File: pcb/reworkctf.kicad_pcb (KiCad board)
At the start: 4 copper layers, 45 x 60 mm, 135 parts, among them J1 XILINX_JTAG, J2 UX60SX-MB-5ST, U1 XC3S50A-4FTG256C, U2 W25Q80BV, U3 74HC04, U4 1 MHz, U5 ADP322ACPZ-145-R7, U6 74HC04

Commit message: Continued initial layout
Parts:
- added G***: LOGO, w_logo:Logo_silk_WEEE_3.4x5mm, F.Cu at (43.0, 21.0)
- added G***: LOGO, w_logo:Logo_silk_ROHS_5x2.8mm, F.Cu at (38.0, 22.0)
- added G***: LOGO, w_logo:Logo_silk_OSHW_6x6mm, F.Cu at (49.0, 20.0)
- added G***: LOGO, azonenberg_pcb:LONGTHING-1200DPI, F.Cu at (33.0, 62.0)
- added R52: 1K, azonenberg_pcb:EIA_0402_RES_NOSILK, F.Cu at (85.6, 52.0)
- added REF**: MECHANICAL_CLEARANCEHOLE_4_40, azonenberg_pcb:MECHANICAL_CLEARANCEHOLE_4_40, F.Cu at (95.0, 71.0)
- added REF**: MECHANICAL_CLEARANCEHOLE_4_40, azonenberg_pcb:MECHANICAL_CLEARANCEHOLE_4_40, F.Cu at (95.0, 21.0)
- C13, C14, C15, C16, C28, C45, R1, R10, R2, R3, R4, R5, R6, R7, R8, R9: moved to B.Cu
- moved R6 88.5 mm to (61.5, 56.5)
- moved R9 78.5 mm to (64.0, 59.0)
- moved R3 73.8 mm to (71.5, 59.5)
- moved R1 71.2 mm to (55.0, 56.0)
- moved R7 68.9 mm to (63.9, 56.5)
- moved R8 68.8 mm to (66.5, 56.5)
- moved R2 68.3 mm to (60.5, 58.0)
- moved R5 64.7 mm to (59.0, 56.0)
- moved R10 62.1 mm to (67.0, 59.5)
- moved R29 59.1 mm to (90.5, 46.5)
- moved R4 59.1 mm to (71.0, 58.0)
- moved C16 52.3 mm to (57.0, 46.0), turned to 180 degrees
- moved C18 52.1 mm to (43.5, 45.5)
- moved C26 47.6 mm to (105.5, 19.5)
- moved C15 46.4 mm to (59.5, 51.5), turned to 180 degrees
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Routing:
- net /GND: track 313.6 -> 317.8 mm, vias 60 -> 62
- net /3V3: track 83.3 -> 85.5 mm
- net /2V5: track 87.2 -> 87.7 mm
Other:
- board size 45 x 60 mm -> 75 x 60 mm
- board text added: "Rework Challenge v0.1 A. Zonenberg / 2017-05-23"

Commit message: Continued work on initial layout
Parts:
- R3, R4, R7, R8: moved to F.Cu
- moved U3 42.0 mm to (83.0, 36.5)
- moved C18 42.0 mm to (83.0, 31.2)
- moved R1 20.0 mm to (55.0, 36.0), turned to 270 degrees
- moved R2 19.8 mm to (57.0, 38.5), turned to 90 degrees
- moved R9 12.9 mm to (55.2, 49.5)
- moved R8 12.1 mm to (54.5, 55.2), turned to 90 degrees
- moved R10 11.7 mm to (56.5, 54.2), turned to 90 degrees
- moved R3 8.56 mm to (72.5, 51.0)
- moved R7 8.00 mm to (56.0, 55.2), turned to 90 degrees
- moved R4 6.60 mm to (65.0, 55.2), turned to 90 degrees
- moved R6 4.07 mm to (57.5, 55.8), turned to 90 degrees
- moved R5 3.16 mm to (58.0, 53.0), turned to 90 degrees
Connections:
- U1 pad C1: /LEVEL22_OK -> /LEVEL1_OK
- U1 pad D1: /LEVEL17_OK -> /LEVEL2_OK
- U1 pad D3: /LEVEL20_OK -> /LEVEL3_OK
- U1 pad D4: /LEVEL19_OK -> /LEVEL9_TEST
- U1 pad E1: /LEVEL18_OK -> /LEVEL4_OK
- U1 pad F1: Net-(R39-Pad2) -> /LEVEL5_OK
- U1 pad F3: /LEVEL9_TEST -> /LEVEL6_OK
- U1 pad G1: /LEVEL8_TEST -> /LEVEL7_OK
- U1 pad G2: /LEVEL15_OK -> /LEVEL8_TEST
- U1 pad G3: Net-(R30-Pad2) -> Net-(U1-PadG3)
- U1 pad H1: /LEVEL16_OK -> /LEVEL8_OK
- U1 pad H3: /LEVEL13_OK -> /LEVEL9_OK
- U1 pad H4: Net-(R38-Pad2) -> Net-(U1-PadH4)
- U1 pad H5: /LEVEL3_TEST -> Net-(U1-PadH5)
- U1 pad H6: Net-(R31-Pad2) -> Net-(U1-PadH6)
- U1 pad J1: /LEVEL12_OK -> /LEVEL10_OK
- U1 pad J3: /LEVEL14_OK -> Net-(U1-PadJ3)
- U1 pad K1: /LEVEL10_OK -> /LEVEL12_OK
- U1 pad K3: /LEVEL9_OK -> /LEVEL13_OK
- U1 pad M1: /LEVEL7_OK -> /LEVEL14_OK
- U1 pad M4: /LEVEL2_OK -> /LEVEL20_OK
- U1 pad N1: /LEVEL8_OK -> /LEVEL15_OK
- U1 pad N2: /LEVEL5_OK -> /LEVEL16_OK
- U1 pad N3: /LEVEL1_OK -> /LEVEL22_OK
- U1 pad P1: /LEVEL6_OK -> /LEVEL17_OK
- U1 pad P2: /LEVEL4_OK -> /LEVEL18_OK
- U1 pad R1: /LEVEL3_OK -> /LEVEL19_OK
- U1 pad R5: Net-(U1-PadR5) -> Net-(R38-Pad2)
- U1 pad R9: Net-(U1-PadR9) -> Net-(R31-Pad2)
- U1 pad T10: Net-(U1-PadT10) -> Net-(R39-Pad2)
- U1 pad T4: Net-(U1-PadT4) -> Net-(R30-Pad2)
- U1 pad T9: Net-(U1-PadT9) -> /LEVEL3_TEST
- U3 pad 8: /LEVEL4_TEST -> /LEVEL4_SENSE
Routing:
- net /JTAG_TDO: track 0.00 -> 46.1 mm, vias 0 -> 3
- net /JTAG_TCK: track 0.00 -> 44.4 mm, vias 0 -> 3
- net /FPGA_DONE: track 0.00 -> 38.4 mm, vias 0 -> 4
- net /LEVEL18_OK: track 0.00 -> 38.2 mm
- net /LEVEL13_OK: track 0.00 -> 37.9 mm
- net /LEVEL19_OK: track 0.00 -> 37.5 mm
- net /LEVEL16_OK: track 0.00 -> 37.2 mm
- net /LEVEL11_OK: track 0.00 -> 36.2 mm
- net /LEVEL17_OK: track 0.00 -> 36.0 mm
- net /LEVEL9_OK: track 0.00 -> 35.9 mm
- net /LEVEL14_OK: track 0.00 -> 35.5 mm
- net /LEVEL12_OK: track 0.00 -> 35.5 mm
- net /LEVEL15_OK: track 0.00 -> 35.2 mm
- net /LEVEL6_OK: track 0.00 -> 34.9 mm
- net /LEVEL10_OK: track 0.00 -> 34.3 mm
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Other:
- board text added: "PCB Rework Challenge v0.1 A. Zonenberg / 2017-05-23"
- board text removed: "Rework Challenge v0.1 A. Zonenberg / 2017-05-23"

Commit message: Began work on active mesh
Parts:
- moved U2 9.33 mm to (82.2, 58.8)
- moved C17 7.52 mm to (87.5, 55.8)
- moved R28 7.52 mm to (86.9, 52.2)
- moved R29 7.52 mm to (92.5, 53.8)
- moved R52 7.52 mm to (87.6, 59.2)
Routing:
- net /GND: track 330.9 -> 540.0 mm, vias 65 -> 163
- net /LEVEL22_OK: track 0.00 -> 27.4 mm, vias 0 -> 1
- net /LEVEL21_OK: track 0.00 -> 26.2 mm, vias 0 -> 1
- net /LEVEL20_OK: track 0.00 -> 24.4 mm, vias 0 -> 1
- net /LEVEL5_OK: track 32.2 -> 50.1 mm
- net /LEVEL2_OK: track 31.0 -> 48.8 mm
- net /LEVEL4_OK: track 32.0 -> 49.6 mm
- net /LEVEL3_OK: track 33.9 -> 51.4 mm
- net /LEVEL1_OK: track 31.2 -> 48.3 mm
- net /SPI_MISO: track 7.75 -> 23.7 mm
- net /SPI_MOSI: track 16.5 -> 31.1 mm
- net /LEVEL6_OK: track 34.9 -> 49.2 mm
- net /LEVEL7_OK: track 33.2 -> 46.7 mm
- net /LEVEL8_OK: track 33.5 -> 46.0 mm
- net /SPI_SCK: track 9.46 -> 21.9 mm
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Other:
- rule via_min_size: 0.55 -> 0.475
- board text added: "PCB Rework Challenge v0.1 A. Zonenberg / 2017-05-24"
- board text removed: "PCB Rework Challenge v0.1 A. Zonenberg / 2017-05-23"

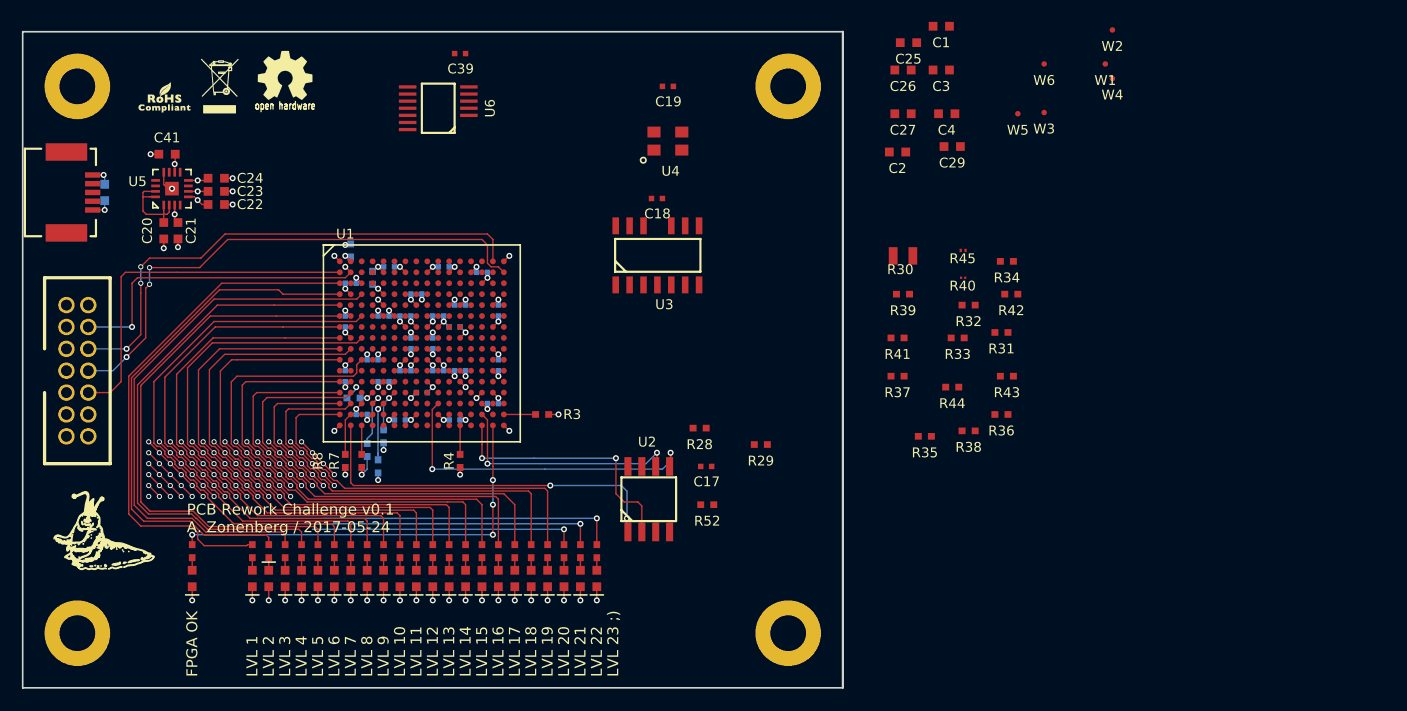
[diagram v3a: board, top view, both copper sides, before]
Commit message: Finished initial work on rework challenge board
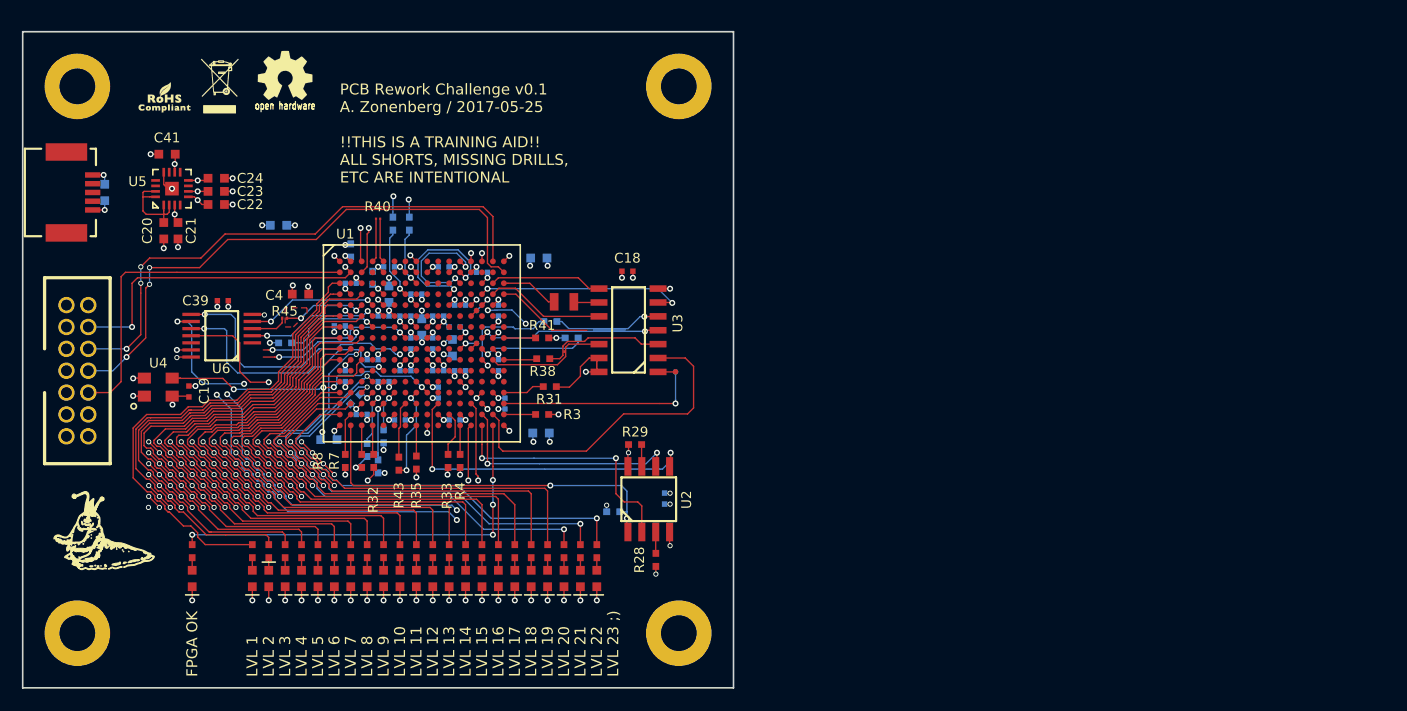
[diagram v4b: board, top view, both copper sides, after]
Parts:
- removed R34: 270, azonenberg_pcb:EIA_0402_RES_NOSILK
- added LEVEL2_SHORT: TESTPOINT_BARETRACE_150UM, azonenberg_pcb:TESTPOINT_BARETRACE_150UM, F.Cu at (77.5, 46.5)
- added LEVEL5_SHORT: TESTPOINT_BARETRACE_150UM, azonenberg_pcb:TESTPOINT_BARETRACE_150UM, F.Cu at (74.5, 45.2)
- added LEVEL6_SHORT: TESTPOINT_BARETRACE_150UM, azonenberg_pcb:TESTPOINT_BARETRACE_150UM, B.Cu at (78.7, 43.3)
- C1, C17, C2, C25, C26, C27, C29, C3, R36, R37, R39, R44, R52, W1, W2, W5: moved to B.Cu
- R41: value 0 -> 270
- R42: value 0 -> 270; moved to B.Cu
- moved C3 65.4 mm to (53.0, 53.3)
- moved W2 63.6 mm to (66.5, 41.5)
- moved W1 62.9 mm to (66.5, 44.5)
- moved R45 62.4 mm to (49.0, 42.2)
- moved W4 61.9 mm to (66.5, 41.5)
- moved C4 61.4 mm to (50.4, 40.0)
- moved R44 61.1 mm to (49.0, 44.5)
- moved C27 58.0 mm to (48.4, 33.7)
- moved R36 56.9 mm to (60.4, 33.5), turned to 270 degrees
- moved R32 56.2 mm to (57.1, 55.2), turned to 90 degrees
- moved R43 56.2 mm to (59.4, 55.5), turned to 90 degrees
- moved W3 56.0 mm to (66.5, 44.5)
- moved R40 53.8 mm to (57.5, 33.1)
- moved C19 51.9 mm to (40.2, 48.9), turned to 90 degrees
- moved U4 51.7 mm to (37.4, 48.5)
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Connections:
- R30 pad 1: /LEVEL4_TEST -> Net-(R30-Pad1)
- R30 pad 2: Net-(R30-Pad2) -> /LEVEL4_TEST
- R32 pad 1: Net-(R32-Pad1) -> /LEVEL16_TEST_A
- R32 pad 2: /LEVEL16_TEST_A -> Net-(R32-Pad2)
- R33 pad 1: Net-(R33-Pad1) -> /LEVEL16_TEST_B
- R33 pad 2: /LEVEL16_TEST_B -> Net-(R33-Pad2)
- R35 pad 1: Net-(R35-Pad1) -> /LEVEL21_TEST
- R35 pad 2: /LEVEL21_TEST -> Net-(R35-Pad2)
- R40 pad 1: /LEVEL9_SENSE -> /LEVEL9_TEST
- R40 pad 2: /LEVEL9_TEST -> /LEVEL9_SENSE
- R41 pad 1: /LEVEL19_SENSE -> Net-(R41-Pad1)
- U1 pad A11: /LEVEL15_TEST_N -> Net-(U1-PadA11)
- U1 pad A12: Net-(U1-PadA12) -> /LEVEL7_TEST_N
- U1 pad A13: Net-(U1-PadA13) -> /LEVEL15_TEST_N
- U1 pad A14: Net-(U1-PadA14) -> /LEVEL15_TEST_P
- U1 pad A3: Net-(U1-PadA3) -> /LEVEL13_TEST_B
- U1 pad A4: Net-(U1-PadA4) -> /LEVEL9_TEST
- U1 pad A5: Net-(U1-PadA5) -> /LEVEL9_SENSE
- U1 pad A8: Net-(U1-PadA8) -> /LEVEL15_TEST_N
- U1 pad B12: Net-(U1-PadB12) -> /LEVEL7_TEST_P
- U1 pad B3: Net-(U1-PadB3) -> /LEVEL13_TEST_A
- U1 pad B8: Net-(U1-PadB8) -> /LEVEL15_TEST_P
- U1 pad C10: /LEVEL15_TEST_N -> Net-(U1-PadC10)
- U1 pad C11: /LEVEL15_TEST_P -> Net-(U1-PadC11)
- U1 pad C13: /LEVEL7_TEST_N -> Net-(U1-PadC13)
- U1 pad C15: Net-(U1-PadC15) -> /LEVEL4_SENSE
- U1 pad C16: Net-(U1-PadC16) -> Net-(R30-Pad1)
- U1 pad C2: /LEVEL21_OK -> Net-(U1-PadC2)
- U1 pad C8: Net-(U1-PadC8) -> Net-(R36-Pad2)
- U1 pad D13: /LEVEL7_TEST_P -> Net-(U1-PadD13)
- U1 pad D14: Net-(U1-PadD14) -> /LEVEL6_SENSE
- U1 pad D15: Net-(U1-PadD15) -> /LEVEL3_SENSE
- U1 pad D16: Net-(U1-PadD16) -> /LEVEL3_TEST
- U1 pad D4: /LEVEL9_TEST -> Net-(U1-PadD4)
- U1 pad D7: Net-(U1-PadD7) -> Net-(R37-Pad2)
- U1 pad D9: /LEVEL15_TEST_P -> Net-(U1-PadD9)
- U1 pad E13: Net-(U1-PadE13) -> /LEVEL19_TEST
- U1 pad E14: Net-(U1-PadE14) -> /LEVEL22_SENSE
- U1 pad E2: /LEVEL11_TEST -> Net-(U1-PadE2)
- U1 pad E3: /LEVEL11_SENSE -> /LEVEL11_TEST
- U1 pad E4: /LEVEL9_SENSE -> /LEVEL11_SENSE
- U1 pad F13: Net-(U1-PadF13) -> /LEVEL22_TEST
- U1 pad H14: Net-(U1-PadH14) -> /LEVEL5_SENSE
- U1 pad H15: Net-(U1-PadH15) -> /LEVEL19_TEST
- U1 pad H16: Net-(U1-PadH16) -> Net-(R41-Pad1)
- U1 pad H7: /LEVEL6_SENSE -> /LEVEL8_SENSE
- U1 pad J14: Net-(U1-PadJ14) -> /LEVEL19_SENSE
- U1 pad J16: /LEVEL22_TEST -> Net-(U1-PadJ16)
- U1 pad J3: Net-(U1-PadJ3) -> /LEVEL20_OK
- U1 pad J7: /LEVEL8_SENSE -> /LEVEL14_SENSE
- U1 pad K14: Net-(R35-Pad1) -> Net-(R39-Pad2)
- U1 pad K15: /LEVEL21_SENSE -> /LEVEL1_SENSE
- U1 pad K16: /LEVEL22_SENSE -> Net-(R38-Pad2)
- U1 pad K5: /LEVEL4_SENSE -> Net-(U1-PadK5)
- U1 pad K6: /LEVEL5_SENSE -> Net-(U1-PadK6)
- U1 pad L10: /LEVEL14_SENSE -> Net-(U1-PadL10)
- U1 pad L5: /LEVEL1_SENSE -> /LEVEL21_SENSE
- U1 pad L6: /LEVEL3_SENSE -> Net-(U1-PadL6)
- U1 pad L7: /LEVEL12_SENSE -> Net-(U1-PadL7)
- U1 pad L8: /LEVEL13_TEST_B -> Net-(U1-PadL8)
- U1 pad L9: /LEVEL13_TEST_A -> Net-(U1-PadL9)
- U1 pad M13: /LEVEL16_TEST_C -> Net-(U1-PadM13)
- U1 pad M14: /LEVEL16_TEST_B -> Net-(U1-PadM14)
- U1 pad M4: /LEVEL20_OK -> /LEVEL21_OK
- U1 pad N11: Net-(R37-Pad2) -> Net-(U1-PadN11)
- U1 pad N13: Net-(R32-Pad1) -> Net-(U1-PadN13)
- U1 pad N16: Net-(U1-PadN16) -> Net-(R31-Pad2)
- U1 pad P11: Net-(R36-Pad2) -> Net-(U1-PadP11)
- U1 pad P13: Net-(U1-PadP13) -> /LEVEL16_TEST_B
- U1 pad P15: Net-(R33-Pad1) -> Net-(U1-PadP15)
- U1 pad P16: /LEVEL16_TEST_A -> /LEVEL12_TEST
- U1 pad P8: /LEVEL19_SENSE -> Net-(U1-PadP8)
- U1 pad R11: /LEVEL14_TEST -> Net-(R33-Pad2)
- U1 pad R15: Net-(R34-Pad1) -> /LEVEL12_SENSE
- U1 pad R5: Net-(R38-Pad2) -> Net-(U1-PadR5)
- U1 pad R9: Net-(R31-Pad2) -> Net-(U1-PadR9)
- U1 pad T10: Net-(R39-Pad2) -> Net-(U1-PadT10)
- U1 pad T13: /LEVEL12_TEST -> /LEVEL16_TEST_A
- U1 pad T4: Net-(R30-Pad2) -> Net-(R32-Pad2)
- U1 pad T5: /LEVEL19_SENSE -> Net-(U1-PadT5)
- U1 pad T6: /LEVEL19_TEST -> Net-(U1-PadT6)
- U1 pad T8: /LEVEL19_TEST -> Net-(R35-Pad2)
- U1 pad T9: /LEVEL3_TEST -> /LEVEL14_TEST
- U3 pad 9: (no net) -> /LEVEL4_TEST
- U6 pad 9: (no net) -> /LEVEL14_TEST
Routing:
- net /GND: track 540.0 -> 694.8 mm, vias 163 -> 193
- net /3V3: track 103.1 -> 202.8 mm, vias 18 -> 33
- net /LEVEL16_TEST_B: track 0.00 -> 71.9 mm, vias 0 -> 4
- net /LEVEL16_TEST_A: track 0.00 -> 58.7 mm, vias 0 -> 4
- net /LEVEL14_TEST: track 0.00 -> 43.5 mm, vias 0 -> 3
- net /LEVEL21_TEST: track 0.00 -> 32.2 mm, vias 0 -> 2
- net /LEVEL12_SENSE: track 0.00 -> 30.2 mm
- net /CLK_1MHZ: track 0.00 -> 25.6 mm, vias 0 -> 4
- net /LEVEL14_SENSE: track 0.00 -> 24.5 mm, vias 0 -> 2
- net /LEVEL21_SENSE: track 0.00 -> 23.2 mm, vias 0 -> 2
- net /LEVEL20_OK: track 24.4 -> 45.6 mm, vias 1 -> 2
- net /LEVEL6_SENSE: track 0.00 -> 19.5 mm, vias 0 -> 2
- net /LEVEL13_TEST_A: track 0.00 -> 18.6 mm, vias 0 -> 4
- net /LEVEL12_TEST: track 0.00 -> 18.6 mm, vias 0 -> 1
- net /LEVEL19_TEST: track 0.00 -> 18.4 mm, vias 0 -> 5
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- added copper zone on In2.Cu, net /1V2
- added copper zone on In2.Cu, net /2V5
- added copper zone on In2.Cu, net /3V3
- added copper zone on In2.Cu, net /5V0
- added copper zone on In1.Cu, net /GND
- added copper zone on F.Cu, net /LEVEL11_TEST
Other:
- board size 75 x 60 mm -> 65 x 60 mm
- board text added: "PCB Rework Challenge v0.1 A. Zonenberg / 2017-05-25 !!THIS IS A TRAINING AID!! ALL SHORTS, MISSING DRILLS, ETC ARE INTENTIONAL"
- board text removed: "PCB Rework Challenge v0.1 A. Zonenberg / 2017-05-24"
